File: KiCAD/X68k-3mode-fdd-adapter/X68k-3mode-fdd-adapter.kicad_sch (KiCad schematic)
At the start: 99 parts, among them J101 4pin, J102 Conn_02x06_Odd_Even, J103 Conn_01x02, J104 Conn_01x04, J105 Conn_01x02, J106 Conn_02x17_Odd_Even, J107 Conn_02x17_Odd_Even, J108 Conn_02x17_Odd_Even, J109 Conn_01x03, Q102 2SC2712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

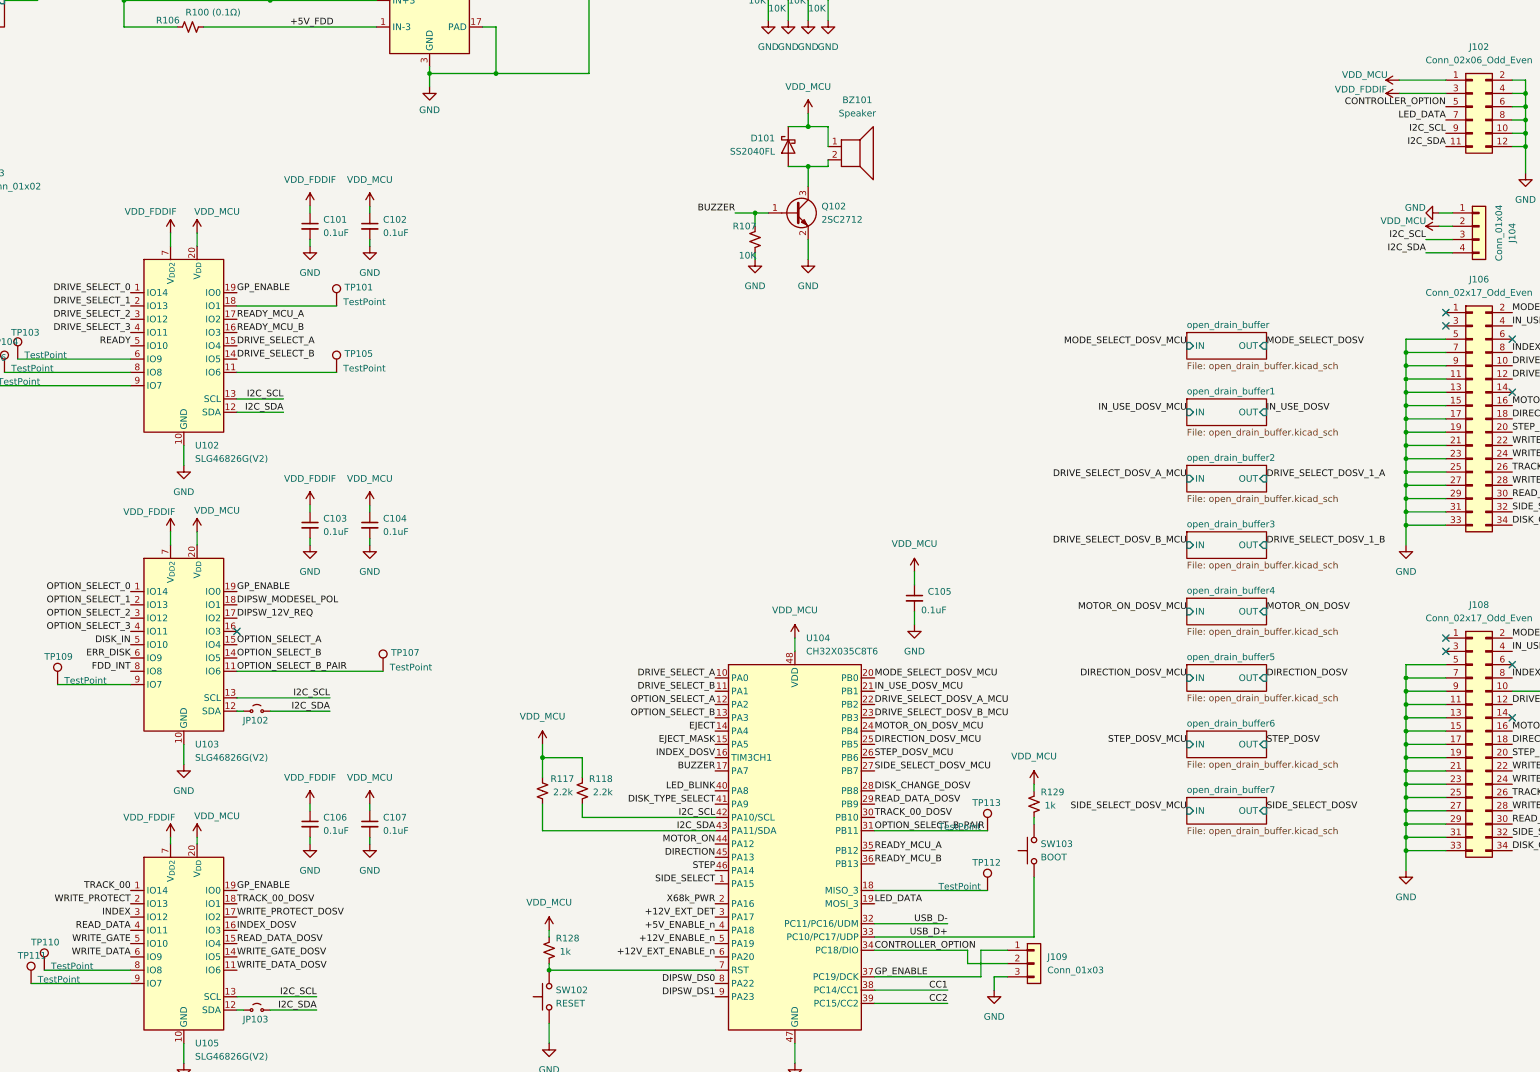
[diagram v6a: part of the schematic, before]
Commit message: * WCH-LinkEを接続できるようにピン配置を変更     * GP_ENABLEをPC6へ     * CONTROLLER_OPTIONを廃止 * Warningを除去 * X68000の電源ONを検出するためにINDEX信号をGP経由で監視できるようにした(GPに専用端子を追加) *
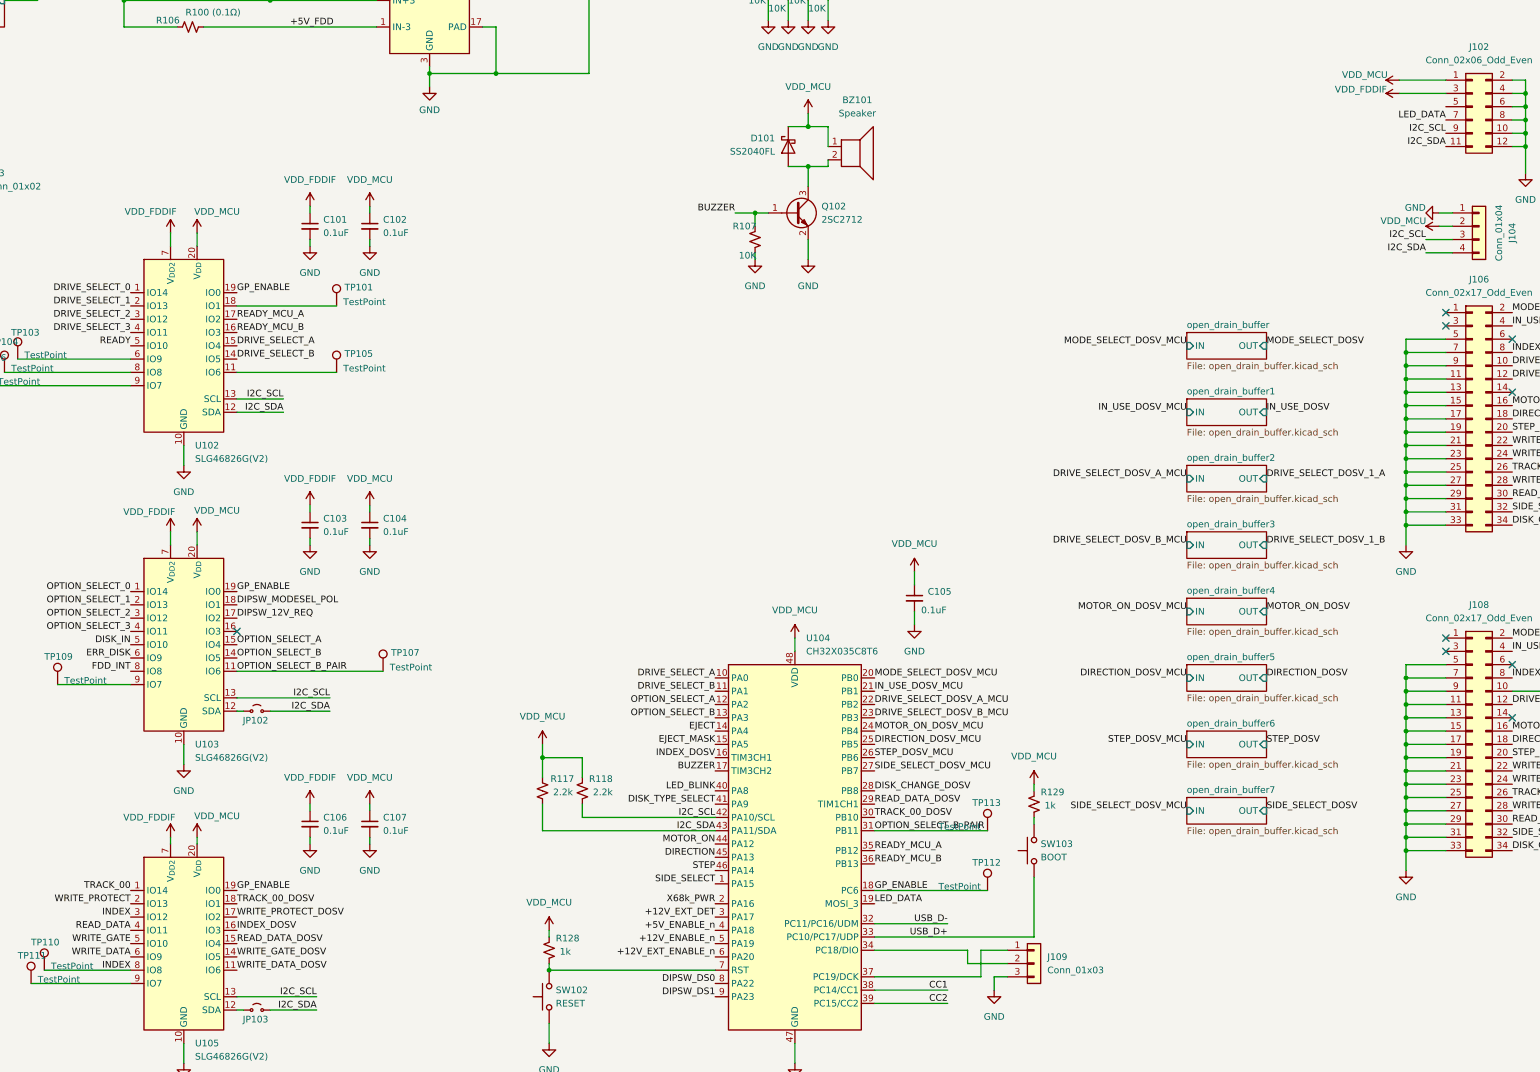
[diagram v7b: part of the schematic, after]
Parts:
- J102: LCSC (none) -> C5333437
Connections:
- net GP_ENABLE: now also TP112.1, U104.18 (PC6); no longer J109.1 (Pin_1), U104.37 (PC19/DCK)
- net INDEX: now also TP110.1, U105.8 (IO8)
- net CONTROLLER_OPTION: no longer names the net of J109.2 (Pin_2), U104.34 (PC18/DIO)
- net CONTROLLER_OPTION: no longer J102.5 (Pin_5)
- new net: J109.1 (Pin_1), U104.37 (PC19/DCK)
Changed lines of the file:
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@@
 		)
 	)
-	(label "CONTROLLER_OPTION"
-		(at 365.76 87.63 180)
-		(effects
-			(font
-				(size 1.27 1.27)
-			)
-			(justify right bottom)
-		)
-	)
 	(label "READY"
 		(at 114.3 133.35 180)
@@
 		)
 	)
-	(label "CONTROLLER_OPTION"
-		(at 256.54 248.92 0)
-		(effects
-			(font
-				(size 1.27 1.27)
-			)
-			(justify left bottom)
-		)
-	)
 	(label "READ_DATA_DOSV"
 		(at 378.46 224.79 0)
@@
 	)
 	(label "GP_ENABLE"
-		(at 256.54 254 0)
+		(at 256.54 237.49 0)
 		(effects
 			(font
@@
 		)
 	)
+	(label "INDEX"
+		(at 114.3 252.73 180)
+		(effects
+			(font
+				(size 1.27 1.27)
+			)
+			(justify right bottom)
+		)
+	)
 	(label "WRITE_DATA"
 		(at 35.56 248.92 180)
@@
 			)
 		)
-		(property "LCIC" ""
-			(at 124.46 246.38 0)
-			(effects
-				(font
-					(size 1.27 1.27)
-				)
-				(hide yes)
-			)
-		)
 		(pin "19"
 		)
@@
 		)
 		(pin "18"
-			(alternate "MISO_3")
 		)
 		(pin "19"
@@
 		)
 		(pin "17"
+			(alternate "TIM3CH2")
 		)
 		(pin "40"
@@
 		)
 		(pin "29"
+			(alternate "TIM1CH1")
 		)
 		(pin "30"
@@
 			)
 		)
-		(property "LCIC" ""
-			(at 124.46 189.23 0)
-			(effects
-				(font
-					(size 1.27 1.27)
-				)
-				(hide yes)
-			)
-		)
 		(pin "19"
 		)
@@
 			)
 		)
-		(property "LCIC" ""
-			(at 124.46 132.08 0)
-			(effects
-				(font
-					(size 1.27 1.27)
-				)
-				(hide yes)
-			)
-		)
 		(pin "19"
 		)
@@
 			)
 		)
-		(property "LCIC" ""
+		(property "LCSC" "C5333437"
 			(at 370.84 87.63 0)
 			(effects
